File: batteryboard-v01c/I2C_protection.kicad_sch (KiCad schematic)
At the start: 18 parts, among them Q6 BSS138DWQ-7, Q7 MBT2222ADW1T1, Q8 BSS138DWQ-7, Q9 MBT2222ADW1T1

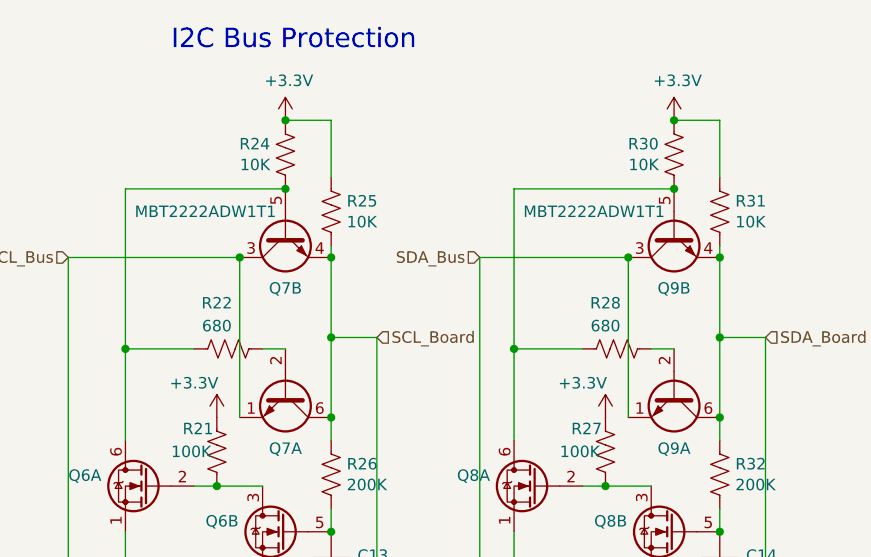
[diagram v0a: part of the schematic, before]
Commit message: updated silkscreen
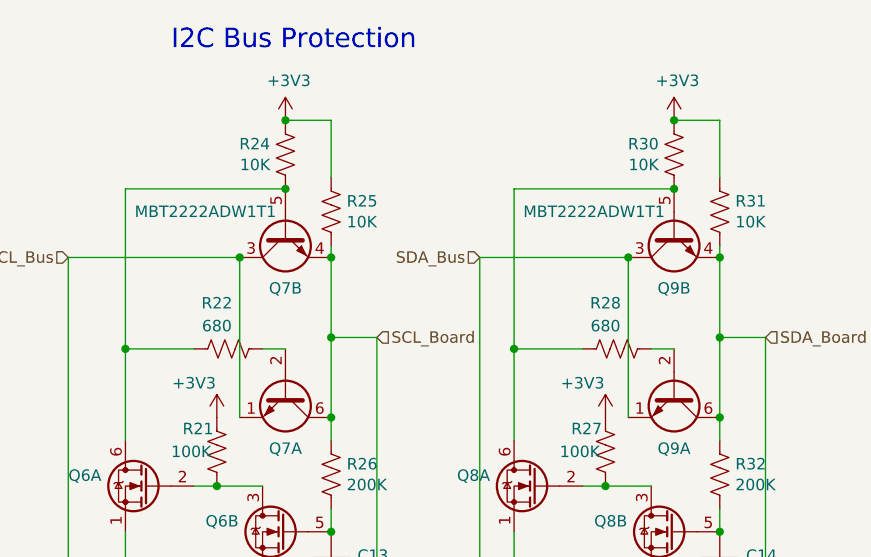
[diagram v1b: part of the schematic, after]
